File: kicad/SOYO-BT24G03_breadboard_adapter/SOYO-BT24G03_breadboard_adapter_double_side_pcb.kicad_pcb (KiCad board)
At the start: 2 copper layers, 26.4 x 62 mm, 4 parts, among them J1 jack, P1 CONN_01X24, P2 CONN_01X23, U1 SOYO-BT24G03

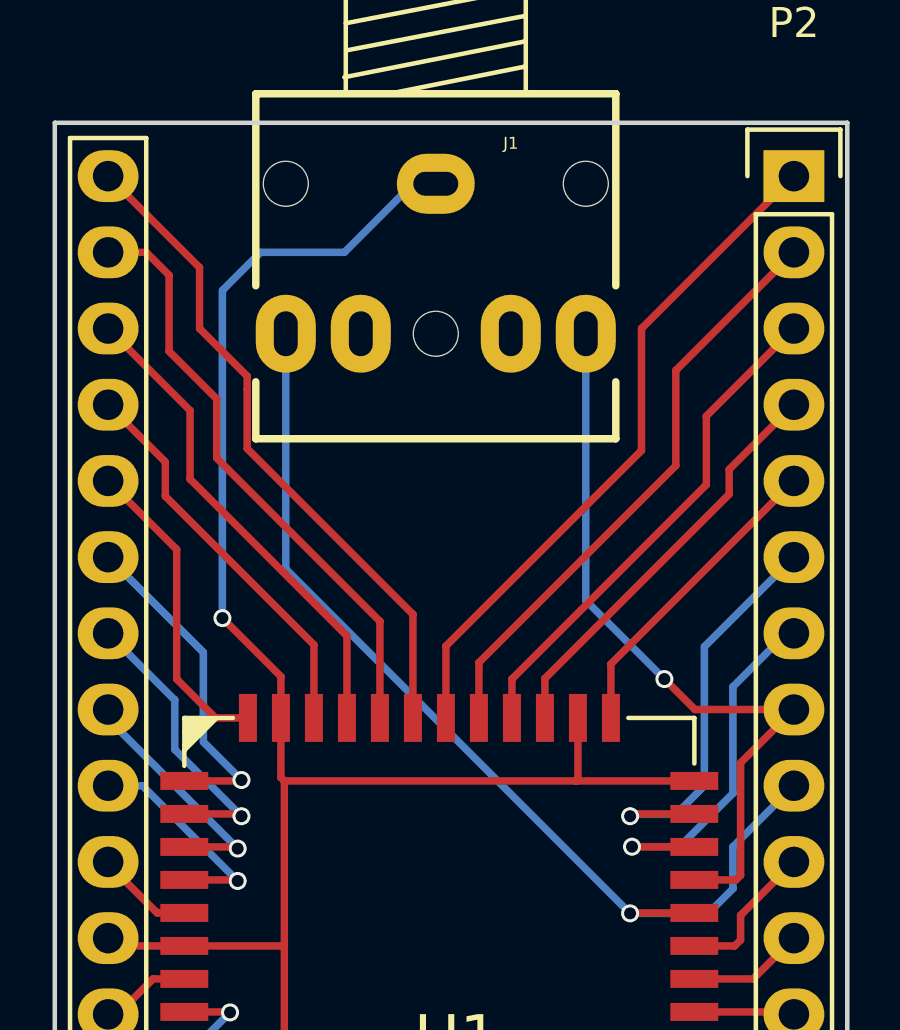
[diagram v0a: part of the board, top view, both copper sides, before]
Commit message: AGND pin separated from GND
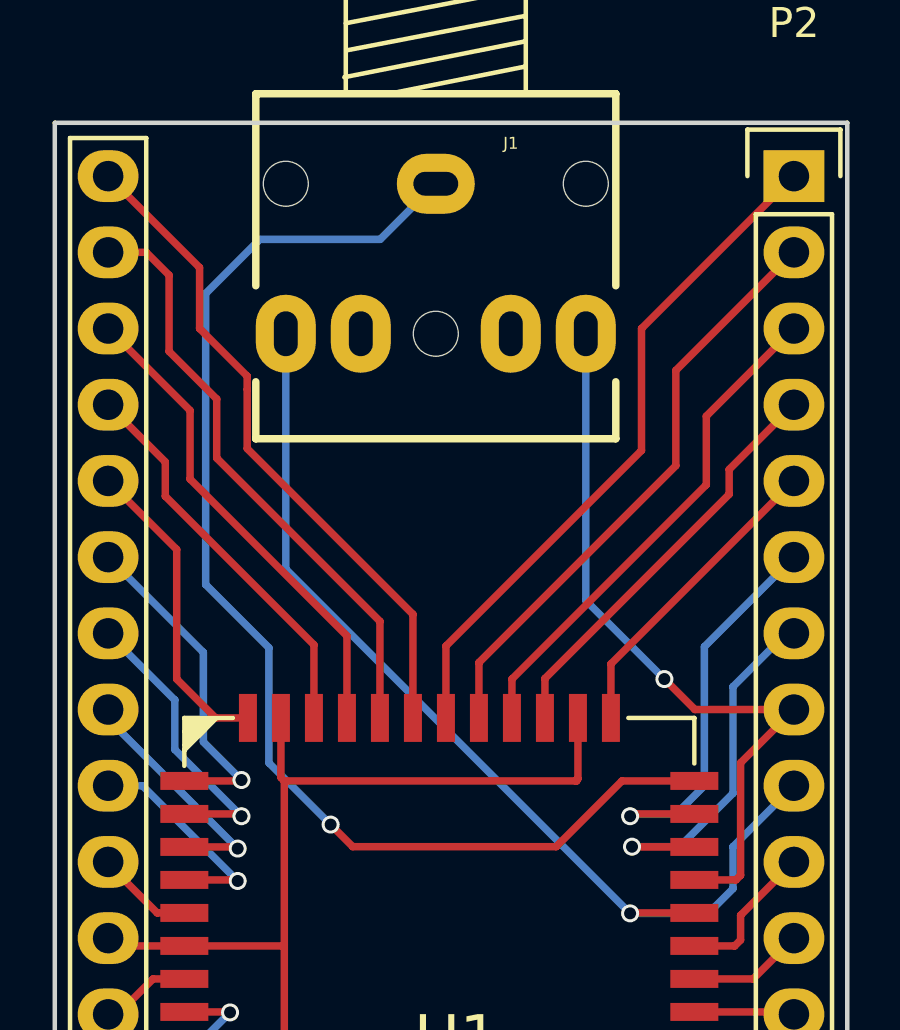
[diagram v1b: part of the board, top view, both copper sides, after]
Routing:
- net Net-(J1-Pad1): track 75.3 -> 89.7 mm
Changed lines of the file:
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@@
-(kicad_pcb (version 4) (host pcbnew 0.201509211831+6205~30~ubuntu14.04.1-product)
+(kicad_pcb (version 20160815) (host pcbnew 4.1.0-alpha+201608211231+7083~46~ubuntu16.04.1-product)
   (general
-    (links 0)
-    (no_connects 0)
-    (area 69.266999 69.266999 95.833001 131.393001)
+    (links 56)
+    (no_connects 1)
+    (area 66.011667 62.098999 99.088334 135.7325)
     (thickness 1.6)
     (drawings 4)
-    (tracks 238)
+    (tracks 241)
     (zones 0)
     (modules 4)
@@
       (hpglpenspeed 20)
       (hpglpendiameter 15)
-      (hpglpenoverlay 2)
       (psnegative false)
       (psa4output false)
@@
     (uvia_dia 0.3)
     (uvia_drill 0.1)
+    (diff_pair_gap 0.25)
+    (diff_pair_width 0.2)
     (add_net "Net-(J1-Pad1)")
     (add_net "Net-(J1-Pad2)")
@@
   (segment (start 82.53 106.68) (end 82.53 115.55) (width 0.25) (layer F.Cu) (net 44))
   (segment (start 82.53 115.55) (end 93.98 127) (width 0.25) (layer F.Cu) (net 44))
-  (segment (start 82.042 71.374) (end 81.28 71.374) (width 0.25) (layer B.Cu) (net 45))
-  (segment (start 81.28 71.374) (end 78.994 73.66) (width 0.25) (layer B.Cu) (net 45))
-  (segment (start 76.2 73.66) (end 74.93 74.93) (width 0.25) (layer B.Cu) (net 45))
-  (segment (start 78.994 73.66) (end 76.2 73.66) (width 0.25) (layer B.Cu) (net 45))
-  (segment (start 76.88 89.18) (end 76.88 87.802) (width 0.25) (layer F.Cu) (net 45))
-  (segment (start 74.93 85.852) (end 74.93 74.93) (width 0.25) (layer B.Cu) (net 45))
-  (via (at 74.93 85.852) (size 0.6) (drill 0.4) (layers F.Cu B.Cu) (net 45))
-  (segment (start 76.88 87.802) (end 74.93 85.852) (width 0.25) (layer F.Cu) (net 45))
+  (segment (start 90.66 91.28) (end 88.2472 91.28) (width 0.25) (layer F.Cu) (net 45) (status 400000))
+  (segment (start 80.1878 73.2282) (end 82.042 71.374) (width 0.25) (layer B.Cu) (net 45) (status 800000))
+  (segment (start 76.1746 73.2282) (end 80.1878 73.2282) (width 0.25) (layer B.Cu) (net 45))
+  (segment (start 74.3712 75.0316) (end 76.1746 73.2282) (width 0.25) (layer B.Cu) (net 45))
+  (segment (start 74.3712 84.7344) (end 74.3712 75.0316) (width 0.25) (layer B.Cu) (net 45))
+  (segment (start 76.4794 86.8426) (end 74.3712 84.7344) (width 0.25) (layer B.Cu) (net 45))
+  (segment (start 76.4794 90.678) (end 76.4794 86.8426) (width 0.25) (layer B.Cu) (net 45))
+  (segment (start 78.5368 92.7354) (end 76.4794 90.678) (width 0.25) (layer B.Cu) (net 45))
+  (via (at 78.5368 92.7354) (size 0.6) (drill 0.4) (layers F.Cu B.Cu) (net 45))
+  (segment (start 79.2734 93.472) (end 78.5368 92.7354) (width 0.25) (layer F.Cu) (net 45))
+  (segment (start 86.0552 93.472) (end 79.2734 93.472) (width 0.25) (layer F.Cu) (net 45))
+  (segment (start 88.2472 91.28) (end 86.0552 93.472) (width 0.25) (layer F.Cu) (net 45))
   (segment (start 83.63 106.68) (end 84.73 106.68) (width 0.25) (layer F.Cu) (net 45))
   (segment (start 84.73 106.68) (end 84.73 103.7165) (width 0.25) (layer F.Cu) (net 45))
@@
   (segment (start 76.88 91.1675) (end 76.88 89.18) (width 0.25) (layer F.Cu) (net 45))
   (segment (start 76.9925 91.28) (end 76.88 91.1675) (width 0.25) (layer F.Cu) (net 45))
-  (segment (start 90.66 91.28) (end 86.741 91.28) (width 0.25) (layer F.Cu) (net 45))
   (segment (start 86.741 91.28) (end 86.708 91.28) (width 0.25) (layer F.Cu) (net 45))
   (segment (start 86.78 91.208) (end 86.78 89.18) (width 0.25) (layer F.Cu) (net 45))
